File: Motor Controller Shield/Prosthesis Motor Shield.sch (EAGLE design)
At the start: 27 parts, among them M1_ACT M02PTH, M2_ACT M02PTH

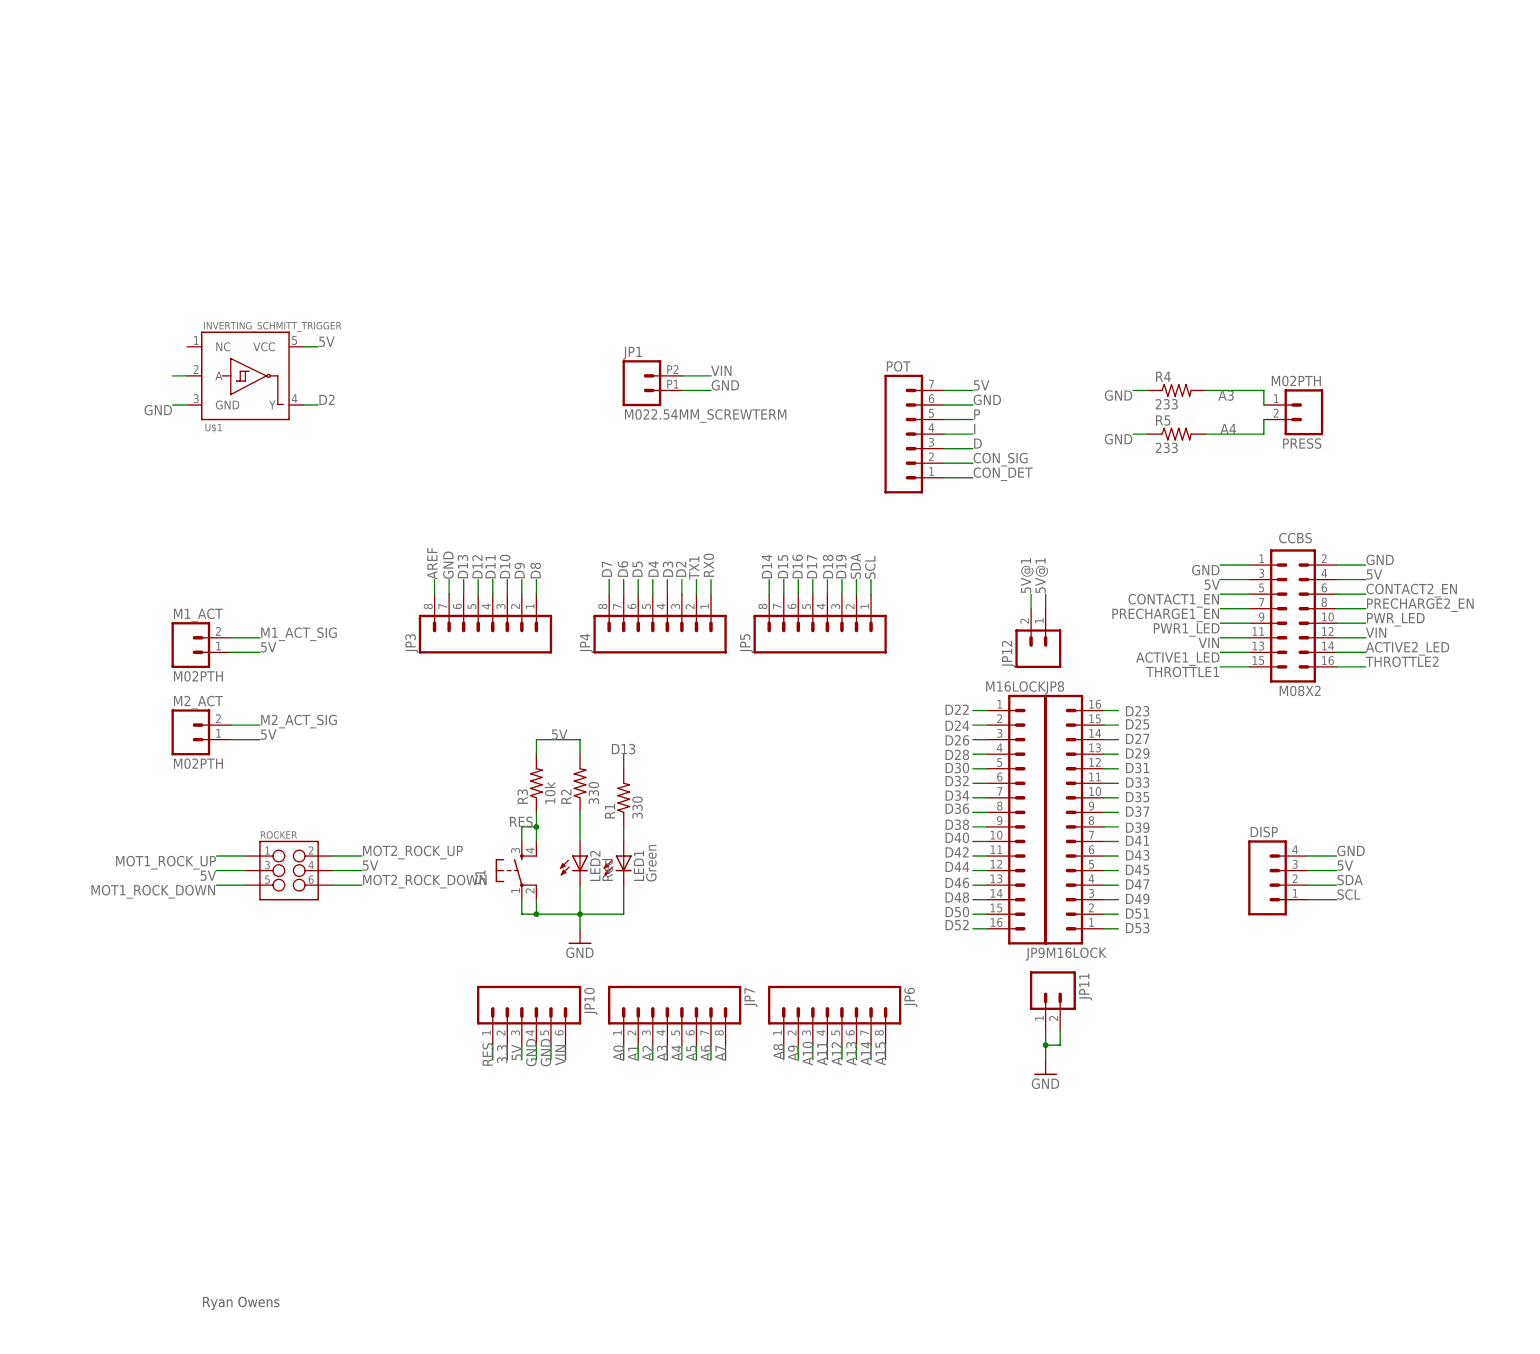
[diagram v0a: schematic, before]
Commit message: Added additional HEX schmitt trigger inverters for debouncing.
Also fixed pin configurations in the MEGA shield. Some were backards.

Connected all of the pin headers to their respective components and
added debouncing for all switch signals.
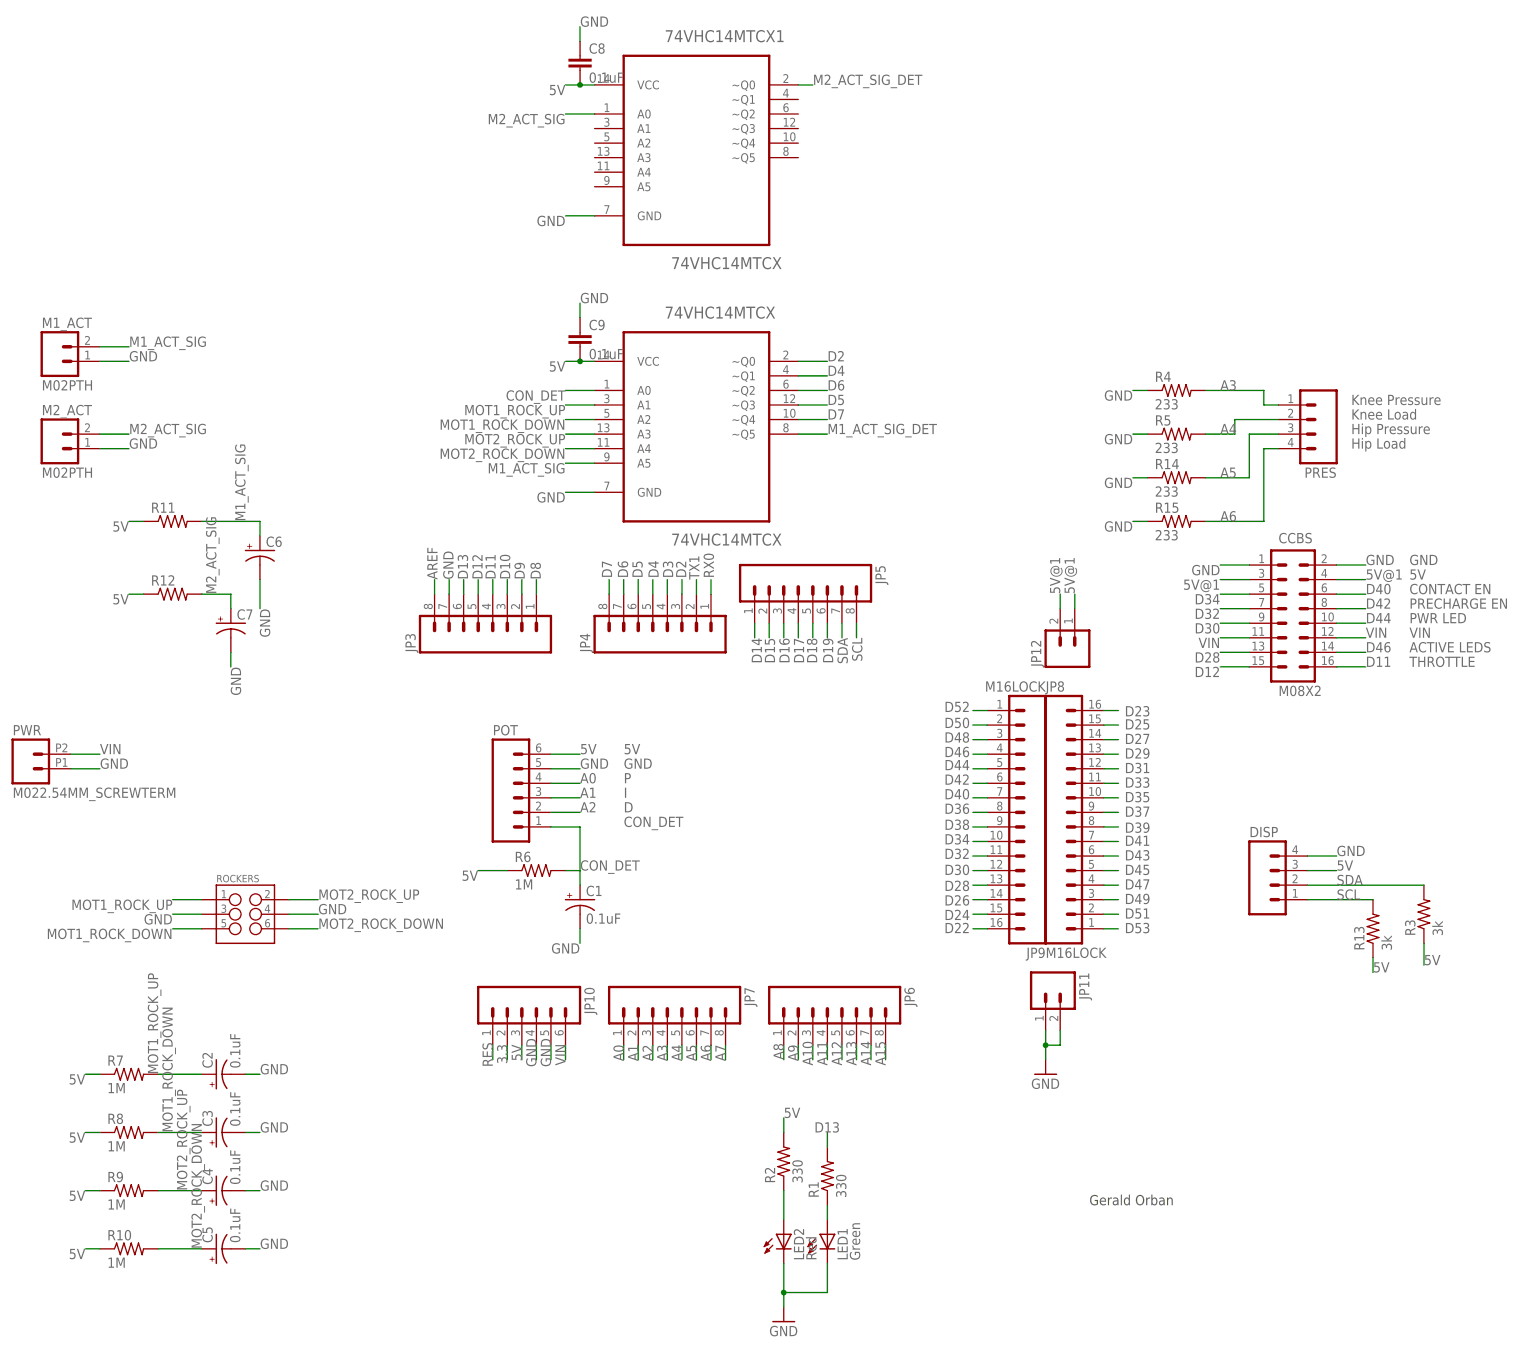
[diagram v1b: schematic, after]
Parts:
- removed JP1: M022.54MM_SCREWTERM, SparkFun-Connectors:M022.54MM_SCREWTERM
- removed PRESS: M02PTH, SparkFun-Connectors:M02PTH
- removed ROCKER: (no value), SparkFun-Connectors:M03X22X3_SILK_SM
- removed S1: (no value), SparkFun:TAC_SWITCHPTH
- removed U$1: INVERTING_SCHMITT_TRIGGER, SparkFun-DigitalIC:INVERTING_SCHMITT_TRIGGER
- added 74VHC14MTCX, 74VHC14MTCX1: 74VHC14MTCX, Fairchild_By_element14_Batch_1:74VHC14MTCX
- added C1, C2, C3, C4, C5: 0.1uF, SparkFun-Capacitors:CAP_POL1206
- added C6, C7: (no value), SparkFun-Capacitors:CAP_POL1206
- added C8, C9: 0.1uF, SparkFun-Capacitors:CAP0603-CAP
- added PRES: (no value), SparkFun-Connectors:M04PTH
- added PWR: M022.54MM_SCREWTERM, SparkFun-Connectors:M022.54MM_SCREWTERM
- added R10, R7, R8, R9: 1M, SparkFun-Resistors:RESISTOR0603
- added R11, R12: (no value), SparkFun-Resistors:RESISTOR0603
- added R13: 3k, SparkFun-Resistors:RESISTOR0603
- added R14, R15: 233, SparkFun-Resistors:RESISTORPTH-1/4W
- added R6: 1M, SparkFun-Resistors:RESISTOR0603-RES
- added ROCKERS: (no value), SparkFun-Connectors:M03X22X3_SILK_SM
- POT: device SparkFun-Connectors:M07 -> SparkFun-Connectors:M06SIP
- R3: value 10k -> 3k; device SparkFun-Passives:RESISTOR0603-RES -> SparkFun-Resistors:RESISTOR0603
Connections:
- removed net ACTIVE1_LED: CCBS.13
- removed net ACTIVE2_LED: CCBS.14
- removed net CONTACT1_EN: CCBS.5
- removed net CONTACT2_EN: CCBS.6
- removed net CON_SIG: POT.2
- removed net D: POT.3
- removed net I: POT.4
- removed net N$1: U$1.A
- removed net P: POT.5
- removed net PRECHARGE1_EN: CCBS.7
- removed net PRECHARGE2_EN: CCBS.8
- removed net PWR1_LED: CCBS.9
- removed net PWR_LED: CCBS.10
- removed net THROTTLE1: CCBS.15
- removed net THROTTLE2: CCBS.16
- new net M1_ACT_SIG_DET: 74VHC14MTCX.~Q5
- new net M2_ACT_SIG_DET: 74VHC14MTCX1.~Q0
- net 5V: now also 74VHC14MTCX.VCC, 74VHC14MTCX1.VCC, C8.2, C9.2, POT.6, R10.1, R11.1, R12.1, R13.1, R3.1, R6.1, R7.1, R8.1, R9.1; no longer CCBS.3, CCBS.4, M1_ACT.1, M2_ACT.1, POT.7, R3.2, ROCKER.3, ROCKER.4, U$1.VCC
- net 5V@1: now also CCBS.3, CCBS.4
- net A0: now also POT.4
- net A1: now also POT.3
- net A2: now also POT.2
- net A3: now also PRES.1; no longer PRESS.1
- net A4: now also PRES.2; no longer PRESS.2
- net A5: now also PRES.3, R14.2
- net A6: now also PRES.4, R15.2
- net CON_DET: now also 74VHC14MTCX.A0, C1.+, R6.2
- net D11: now also CCBS.16
- net D12: now also CCBS.15
- net D14: now also JP5.1; no longer JP5.8
- net D15: now also JP5.2; no longer JP5.7
- net D16: now also JP5.3; no longer JP5.6
- net D17: now also JP5.4; no longer JP5.5
- net D18: now also JP5.5; no longer JP5.4
- net D19: now also JP5.6; no longer JP5.3
- net D2: now also 74VHC14MTCX.~Q0; no longer U$1.Y
- net D22: now also JP9.16; no longer JP9.1
- net D24: now also JP9.15; no longer JP9.2
- net D26: now also JP9.14; no longer JP9.3
- net D28: now also CCBS.13, JP9.13; no longer JP9.4
- net D30: now also CCBS.9, JP9.12; no longer JP9.5
- net D32: now also CCBS.7, JP9.11; no longer JP9.6
- net D34: now also CCBS.5, JP9.10; no longer JP9.7
- net D36: now also JP9.9; no longer JP9.8
- net D38: now also JP9.8; no longer JP9.9
- net D4: now also 74VHC14MTCX.~Q1
- net D40: now also CCBS.6, JP9.7; no longer JP9.10
- net D42: now also CCBS.8, JP9.6; no longer JP9.11
- net D44: now also CCBS.10, JP9.5; no longer JP9.12
- net D46: now also CCBS.14, JP9.4; no longer JP9.13
- net D48: now also JP9.3; no longer JP9.14
- net D5: now also 74VHC14MTCX.~Q3
- net D50: now also JP9.2; no longer JP9.15
- net D52: now also JP9.1; no longer JP9.16
- net D6: now also 74VHC14MTCX.~Q2
- net D7: now also 74VHC14MTCX.~Q4
- net GND: now also 74VHC14MTCX.GND, 74VHC14MTCX1.GND, C1.-, C2.-, C3.-, C4.-, C5.-, C6.-, C7.-, C8.1, C9.1, M1_ACT.1, M2_ACT.1, POT.5, PWR.1, R14.1, R15.1, ROCKERS.3, ROCKERS.4; no longer JP1.1, POT.6, S1.1, S1.2, U$1.GND
- net M1_ACT_SIG: now also 74VHC14MTCX.A5, C6.+, R11.2
- net M2_ACT_SIG: now also 74VHC14MTCX1.A0, C7.+, R12.2
- net MOT1_ROCK_DOWN: now also 74VHC14MTCX.A2, C3.+, R8.2, ROCKERS.5; no longer ROCKER.5
- net MOT1_ROCK_UP: now also 74VHC14MTCX.A1, C2.+, R7.2, ROCKERS.1; no longer ROCKER.1
- net MOT2_ROCK_DOWN: now also 74VHC14MTCX.A4, C5.+, R10.2, ROCKERS.6; no longer ROCKER.6
- net MOT2_ROCK_UP: now also 74VHC14MTCX.A3, C4.+, R9.2, ROCKERS.2; no longer ROCKER.2
- net RES: no longer R3.1, S1.3, S1.4
- net SCL: now also JP5.8, R13.2; no longer JP5.1
- net SDA: now also JP5.7, R3.2; no longer JP5.2
- net VIN: now also PWR.2; no longer JP1.2
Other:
- note added: "5V"
- note added: "ACTIVE LEDS"
- note added: "CONTACT EN"
- note added: "CON_DET"
- note added: "D"
- note added: "GND"
- note added: "Gerald Orban"
- note added: "Hip Load"
- note added: "Hip Pressure"
- note added: "I"
- note added: "Knee Load"
- note added: "Knee Pressure"
- note added: "P"
- note added: "PRECHARGE EN"
- note added: "PWR LED"
- note added: "THROTTLE"
- note added: "VIN"
- note removed: "Ryan Owens"
- moved on the sheet: JP12, JP5, LED1, LED2, M1_ACT, M2_ACT, R1, R2, R3

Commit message: Incremental changes for layout.
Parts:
- renumbered PRES to PRES_INPUT
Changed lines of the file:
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@@
 <part name="POT" library="SparkFun-Connectors" deviceset="M06" device="SIP"/>
 <part name="74VHC14MTCX1" library="Fairchild_By_element14_Batch_1" deviceset="74VHC14MTCX" device=""/>
-<part name="PRES" library="SparkFun-Connectors" deviceset="M04" device="PTH"/>
+<part name="PRES_INPUT" library="SparkFun-Connectors" deviceset="M04" device="PTH"/>
 <part name="R14" library="SparkFun-Resistors" deviceset="RESISTOR" device="PTH-1/4W" value="233"/>
 <part name="R15" library="SparkFun-Resistors" deviceset="RESISTOR" device="PTH-1/4W" value="233"/>
@@
 <instance part="POT" gate="G$1" x="86.36" y="99.06"/>
 <instance part="74VHC14MTCX1" gate="A" x="116.84" y="215.9"/>
-<instance part="PRES" gate="G$1" x="223.52" y="165.1" rot="R180"/>
+<instance part="PRES_INPUT" gate="G$1" x="223.52" y="165.1" rot="R180"/>
 <instance part="R14" gate="G$1" x="200.66" y="154.94"/>
 <instance part="R15" gate="G$1" x="200.66" y="147.32"/>
@@
 </segment>
 <segment>
-<pinref part="DISP" gate="G$1" pin="3"/>
-<wire x1="223.52" y1="86.36" x2="228.6" y2="86.36" width="0.2032" layer="91"/>
-<label x="228.6" y="86.36" size="1.778" layer="95"/>
-</segment>
-<segment>
 <pinref part="74VHC14MTCX" gate="A" pin="VCC"/>
 <wire x1="99.06" y1="175.26" x2="96.52" y2="175.26" width="0.2032" layer="91"/>
@@
 </segment>
 <segment>
-<pinref part="R13" gate="G$1" pin="1"/>
-<wire x1="234.95" y1="71.12" x2="234.95" y2="68.58" width="0.2032" layer="91"/>
-<label x="234.95" y="68.58" size="1.778" layer="95"/>
-</segment>
-<segment>
-<pinref part="R3" gate="G$1" pin="1"/>
-<wire x1="243.84" y1="73.66" x2="243.84" y2="69.85" width="0.2032" layer="91"/>
-<label x="243.84" y="69.85" size="1.778" layer="95"/>
-</segment>
-<segment>
 <pinref part="74VHC14MTCX1" gate="A" pin="VCC"/>
 <wire x1="99.06" y1="223.52" x2="96.52" y2="223.52" width="0.2032" layer="91"/>
@@
 <wire x1="96.52" y1="223.52" x2="93.98" y2="223.52" width="0.2032" layer="91"/>
 <junction x="96.52" y="223.52"/>
+</segment>
+<segment>
+<pinref part="DISP" gate="G$1" pin="3"/>
+<wire x1="223.52" y1="86.36" x2="228.6" y2="86.36" width="0.2032" layer="91"/>
+<label x="228.6" y="86.36" size="1.778" layer="95"/>
+</segment>
+<segment>
+<pinref part="R3" gate="G$1" pin="1"/>
+<wire x1="243.84" y1="73.66" x2="243.84" y2="69.85" width="0.2032" layer="91"/>
+<label x="243.84" y="69.85" size="1.778" layer="95"/>
+</segment>
+<segment>
+<pinref part="R13" gate="G$1" pin="1"/>
+<wire x1="234.95" y1="71.12" x2="234.95" y2="68.58" width="0.2032" layer="91"/>
+<label x="234.95" y="68.58" size="1.778" layer="95"/>
 </segment>
 </net>
@@
 <wire x1="215.9" y1="170.18" x2="215.9" y2="167.64" width="0.2032" layer="91"/>
 <label x="208.28" y="170.18" size="1.778" layer="95"/>
-<pinref part="PRES" gate="G$1" pin="1"/>
+<pinref part="PRES_INPUT" gate="G$1" pin="1"/>
 <wire x1="215.9" y1="167.64" x2="218.44" y2="167.64" width="0.2032" layer="91"/>
 </segment>
@@
 <wire x1="210.82" y1="162.56" x2="205.74" y2="162.56" width="0.2032" layer="91"/>
 <label x="208.28" y="162.56" size="1.778" layer="95"/>
-<pinref part="PRES" gate="G$1" pin="2"/>
+<pinref part="PRES_INPUT" gate="G$1" pin="2"/>
 <wire x1="210.82" y1="165.1" x2="218.44" y2="165.1" width="0.2032" layer="91"/>
 </segment>
@@
 <wire x1="205.74" y1="154.94" x2="213.36" y2="154.94" width="0.2032" layer="91"/>
 <wire x1="213.36" y1="154.94" x2="213.36" y2="162.56" width="0.2032" layer="91"/>
-<pinref part="PRES" gate="G$1" pin="3"/>
+<pinref part="PRES_INPUT" gate="G$1" pin="3"/>
 <wire x1="213.36" y1="162.56" x2="218.44" y2="162.56" width="0.2032" layer="91"/>
 <label x="208.28" y="154.94" size="1.778" layer="95"/>
@@
 <wire x1="205.74" y1="147.32" x2="215.9" y2="147.32" width="0.2032" layer="91"/>
 <wire x1="215.9" y1="147.32" x2="215.9" y2="160.02" width="0.2032" layer="91"/>
-<pinref part="PRES" gate="G$1" pin="4"/>
+<pinref part="PRES_INPUT" gate="G$1" pin="4"/>
 <wire x1="215.9" y1="160.02" x2="218.44" y2="160.02" width="0.2032" layer="91"/>
 <label x="208.28" y="147.32" size="1.778" layer="95"/>

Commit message: Splitting M1 and M2 debouncing signals between the inverters
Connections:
- removed net M1_ACT_SIG_DET: 74VHC14MTCX.~Q5
- removed net M2_ACT_SIG_DET: 74VHC14MTCX1.~Q0
- net D26: now also 74VHC14MTCX.~Q5
- net D48: now also 74VHC14MTCX1.~Q0
- net D5: now also 74VHC14MTCX1.~Q1; no longer 74VHC14MTCX.~Q3
- net D7: now also 74VHC14MTCX1.~Q2; no longer 74VHC14MTCX.~Q4
- net MOT2_ROCK_DOWN: now also 74VHC14MTCX1.A2; no longer 74VHC14MTCX.A4
- net MOT2_ROCK_UP: now also 74VHC14MTCX1.A1; no longer 74VHC14MTCX.A3
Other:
- note added: "M1_ACT_SIG_DET"
- note added: "M2_ACT_SIG_DET"
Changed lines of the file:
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@@
 <text x="231.14" y="162.56" size="1.778" layer="95">Hip Pressure</text>
 <text x="231.14" y="160.02" size="1.778" layer="95">Hip Load</text>
+<text x="144.78" y="223.52" size="1.778" layer="95">M2_ACT_SIG_DET</text>
+<text x="147.32" y="162.56" size="1.778" layer="95">M1_ACT_SIG_DET</text>
 </plain>
 <instances>
@@
 </segment>
 <segment>
-<pinref part="74VHC14MTCX" gate="A" pin="~Q3"/>
-<wire x1="134.62" y1="167.64" x2="139.7" y2="167.64" width="0.2032" layer="91"/>
-<label x="139.7" y="167.64" size="1.778" layer="95"/>
+<pinref part="74VHC14MTCX1" gate="A" pin="~Q1"/>
+<wire x1="134.62" y1="220.98" x2="137.16" y2="220.98" width="0.2032" layer="91"/>
+<label x="137.16" y="220.98" size="1.778" layer="95"/>
 </segment>
 </net>
@@
 </segment>
 <segment>
-<pinref part="74VHC14MTCX" gate="A" pin="~Q4"/>
-<wire x1="134.62" y1="165.1" x2="139.7" y2="165.1" width="0.2032" layer="91"/>
-<label x="139.7" y="165.1" size="1.778" layer="95"/>
+<pinref part="74VHC14MTCX1" gate="A" pin="~Q2"/>
+<wire x1="134.62" y1="218.44" x2="137.16" y2="218.44" width="0.2032" layer="91"/>
+<label x="137.16" y="218.44" size="1.778" layer="95"/>
 </segment>
 </net>
@@
 <pinref part="JP9" gate="G$1" pin="14"/>
 </segment>
+<segment>
+<pinref part="74VHC14MTCX" gate="A" pin="~Q5"/>
+<wire x1="134.62" y1="162.56" x2="139.7" y2="162.56" width="0.2032" layer="91"/>
+<label x="139.7" y="162.56" size="1.778" layer="95"/>
+</segment>
 </net>
 <net name="D28" class="0">
@@
 <label x="164.592" y="110.49" size="1.778" layer="95" rot="R180"/>
 <pinref part="JP9" gate="G$1" pin="3"/>
+</segment>
+<segment>
+<pinref part="74VHC14MTCX1" gate="A" pin="~Q0"/>
+<wire x1="134.62" y1="223.52" x2="137.16" y2="223.52" width="0.2032" layer="91"/>
+<label x="137.16" y="223.52" size="1.778" layer="95"/>
 </segment>
 </net>
@@
 </segment>
 <segment>
-<pinref part="74VHC14MTCX" gate="A" pin="A3"/>
-<wire x1="99.06" y1="162.56" x2="93.98" y2="162.56" width="0.2032" layer="91"/>
-<label x="93.98" y="162.56" size="1.778" layer="95" rot="R180"/>
+<pinref part="74VHC14MTCX1" gate="A" pin="A1"/>
+<wire x1="99.06" y1="215.9" x2="93.98" y2="215.9" width="0.2032" layer="91"/>
+<label x="93.98" y="215.9" size="1.778" layer="95" rot="R180"/>
 </segment>
 </net>
@@
 </segment>
 <segment>
-<pinref part="74VHC14MTCX" gate="A" pin="A4"/>
-<wire x1="99.06" y1="160.02" x2="93.98" y2="160.02" width="0.2032" layer="91"/>
-<label x="93.98" y="160.02" size="1.778" layer="95" rot="R180"/>
+<pinref part="74VHC14MTCX1" gate="A" pin="A2"/>
+<wire x1="99.06" y1="213.36" x2="93.98" y2="213.36" width="0.2032" layer="91"/>
+<label x="93.98" y="213.36" size="1.778" layer="95" rot="R180"/>
 </segment>
 </net>
@@
 </segment>
 </net>
-<net name="M1_ACT_SIG_DET" class="0">
-<segment>
-<pinref part="74VHC14MTCX" gate="A" pin="~Q5"/>
-<wire x1="134.62" y1="162.56" x2="139.7" y2="162.56" width="0.2032" layer="91"/>
-<label x="139.7" y="162.56" size="1.778" layer="95"/>
-</segment>
-</net>
-<net name="M2_ACT_SIG_DET" class="0">
-<segment>
-<pinref part="74VHC14MTCX1" gate="A" pin="~Q0"/>
-<wire x1="134.62" y1="223.52" x2="137.16" y2="223.52" width="0.2032" layer="91"/>
-<label x="137.16" y="223.52" size="1.778" layer="95"/>
-</segment>
-</net>
